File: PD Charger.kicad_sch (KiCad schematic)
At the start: 76 parts, among them J1 USB_C_Receptacle_USB2.0, J2 Conn_ARM_SWD_TagConnect_TC2030, J3 XT60_M, Q1 NMOS, Q2 NMOS, Q3 NMOS, Q4 NMOS, Q5 NTMFS002P03, Q6 NTMFS002P03, Q7 Q_Dual_NMOS_S1G1D2S2G2D1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

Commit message: values updated
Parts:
- C1: value Cin -> 82u
- C14, C15, C16, C17: value Cin -> 10u
- C18, C19, C20, C21, C27, C28: value Cout -> 10u
- C2: value Cout -> 82u
- C3, C4: value C -> 0.47u
- C34: value FF -> 20p
- J3: footprint Connector_AMASS:AMASS_XT60IPW-M_1x03_P7.20mm_Horizontal -> Connector_AMASS:AMASS_XT60PW-M_1x02_P7.20mm_Horizontal
- R1, R2, R3, R4: value R -> 1
- R10, R7: value Rup -> 100k
- R11: value Rdiv1 -> 36k
- R12: value Rdiv2 -> 9k
- R14, R17: value R -> 100k
- R15: value R -> 752
- R16, R18: value R -> 5820
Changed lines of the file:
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@@
       (effects (font (size 1.27 1.27)) (justify left))
     )
-    (property "Value" "Cout" (at 249.682 140.97 0)
+    (property "Value" "10u" (at 249.682 140.97 0)
       (effects (font (size 1.27 1.27)) (justify left))
     )
@@
       (effects (font (size 1.27 1.27)))
     )
-    (property "Value" "R" (at 81.28 59.69 90)
+    (property "Value" "1" (at 81.28 59.69 90)
       (effects (font (size 1.27 1.27)))
     )
@@
       (effects (font (size 1.27 1.27)))
     )
-    (property "Footprint" "Connector_AMASS:AMASS_XT60IPW-M_1x03_P7.20mm_Horizontal" (at 141.732 41.91 0)
+    (property "Footprint" "Connector_AMASS:AMASS_XT60PW-M_1x02_P7.20mm_Horizontal" (at 141.732 41.91 0)
       (effects (font (size 1.27 1.27)) hide)
     )
@@
       (effects (font (size 1.27 1.27)) (justify left))
     )
-    (property "Value" "Cin" (at 184.15 41.91 0)
+    (property "Value" "82u" (at 184.15 41.91 0)
       (effects (font (size 1.27 1.27)) (justify left))
     )
@@
       (effects (font (size 1.27 1.27)) (justify left))
     )
-    (property "Value" "Cout" (at 239.014 140.97 0)
+    (property "Value" "10u" (at 239.014 140.97 0)
       (effects (font (size 1.27 1.27)) (justify left))
     )
@@
       (effects (font (size 1.27 1.27)) (justify left))
     )
-    (property "Value" "R" (at 102.489 103.124 0)
+    (property "Value" "100k" (at 102.489 103.124 0)
       (effects (font (size 1.27 1.27)) (justify left))
     )
@@
       (effects (font (size 1.27 1.27)) (justify left))
     )
-    (property "Value" "Cout" (at 278.13 41.91 0)
+    (property "Value" "10u" (at 278.13 41.91 0)
       (effects (font (size 1.27 1.27)) (justify left))
     )
@@
       (effects (font (size 1.27 1.27)) (justify left))
     )
-    (property "Value" "R" (at 102.489 111.76 0)
+    (property "Value" "5820" (at 102.489 111.76 0)
       (effects (font (size 1.27 1.27)) (justify left))
     )
@@
       (effects (font (size 1.27 1.27)))
     )
-    (property "Value" "Rdiv1" (at 111.76 47.752 90)
+    (property "Value" "36k" (at 111.76 47.752 90)
       (effects (font (size 1.27 1.27)))
     )
@@
       (effects (font (size 1.27 1.27)) (justify left))
     )
-    (property "Value" "Cin" (at 176.53 41.91 0)
+    (property "Value" "10u" (at 176.53 41.91 0)
       (effects (font (size 1.27 1.27)) (justify left))
     )
@@
       (effects (font (size 1.27 1.27)) (justify left))
     )
-    (property "Value" "Cout" (at 255.27 41.91 0)
+    (property "Value" "10u" (at 255.27 41.91 0)
       (effects (font (size 1.27 1.27)) (justify left))
     )
@@
       (effects (font (size 1.27 1.27)) (justify left))
     )
-    (property "Value" "Cout" (at 247.65 41.91 0)
+    (property "Value" "82u" (at 247.65 41.91 0)
       (effects (font (size 1.27 1.27)) (justify left))
     )
@@
       (effects (font (size 1.27 1.27)))
     )
-    (property "Value" "R" (at 81.28 22.86 90)
+    (property "Value" "1" (at 81.28 22.86 90)
       (effects (font (size 1.27 1.27)))
     )
@@
       (effects (font (size 1.27 1.27)) (justify left))
     )
-    (property "Value" "Cin" (at 162.56 41.91 0)
+    (property "Value" "10u" (at 162.56 41.91 0)
       (effects (font (size 1.27 1.27)) (justify left))
     )
@@
       (effects (font (size 1.27 1.27)) (justify left))
     )
-    (property "Value" "C" (at 97.79 52.07 0)
+    (property "Value" "0.47u" (at 97.79 52.07 0)
       (effects (font (size 1.27 1.27)) (justify left))
     )
@@
       (effects (font (size 1.27 1.27)))
     )
-    (property "Value" "Rdiv2" (at 111.76 56.388 90)
+    (property "Value" "9k" (at 111.76 56.388 90)
       (effects (font (size 1.27 1.27)))
     )
@@
       (effects (font (size 1.27 1.27)) (justify left))
     )
-    (property "Value" "Rup" (at 49.53 25.4 0)
+    (property "Value" "100k" (at 49.53 25.4 0)
       (effects (font (size 1.27 1.27)) (justify left))
     )
@@
       (effects (font (size 1.27 1.27)) (justify left))
     )
-    (property "Value" "Cout" (at 270.51 41.91 0)
+    (property "Value" "10u" (at 270.51 41.91 0)
       (effects (font (size 1.27 1.27)) (justify left))
     )
@@
       (effects (font (size 1.27 1.27)) (justify left))
     )
-    (property "Value" "FF" (at 219.456 154.178 0)
+    (property "Value" "20p" (at 219.456 154.178 0)
       (effects (font (size 1.27 1.27)) (justify left))
     )
@@
       (effects (font (size 1.27 1.27)))
     )
-    (property "Value" "R" (at 81.28 40.64 90)
+    (property "Value" "1" (at 81.28 40.64 90)
       (effects (font (size 1.27 1.27)))
     )
@@
       (effects (font (size 1.27 1.27)) (justify left))
     )
-    (property "Value" "R" (at 115.697 103.124 0)
+    (property "Value" "100k" (at 115.697 103.124 0)
       (effects (font (size 1.27 1.27)) (justify left))
     )
@@
       (effects (font (size 1.27 1.27)) (justify left))
     )
-    (property "Value" "Cin" (at 156.21 41.91 0)
+    (property "Value" "10u" (at 156.21 41.91 0)
       (effects (font (size 1.27 1.27)) (justify left))
     )
@@
       (effects (font (size 1.27 1.27)) (justify left))
     )
-    (property "Value" "Cout" (at 262.89 41.91 0)
+    (property "Value" "10u" (at 262.89 41.91 0)
       (effects (font (size 1.27 1.27)) (justify left))
     )
@@
       (effects (font (size 1.27 1.27)))
     )
-    (property "Value" "R" (at 81.28 52.07 90)
+    (property "Value" "1" (at 81.28 52.07 90)
       (effects (font (size 1.27 1.27)))
     )
@@
       (effects (font (size 1.27 1.27)) (justify left))
     )
-    (property "Value" "Cin" (at 168.91 41.91 0)
+    (property "Value" "10u" (at 168.91 41.91 0)
       (effects (font (size 1.27 1.27)) (justify left))
     )
@@
       (effects (font (size 1.27 1.27)) (justify left))
     )
-    (property "Value" "R" (at 115.697 111.76 0)
+    (property "Value" "5820" (at 115.697 111.76 0)
       (effects (font (size 1.27 1.27)) (justify left))
     )
@@
       (effects (font (size 1.27 1.27)) (justify left))
     )
-    (property "Value" "C" (at 97.79 34.29 0)
+    (property "Value" "0.47u" (at 97.79 34.29 0)
       (effects (font (size 1.27 1.27)) (justify left))
     )
@@
       (effects (font (size 1.27 1.27)))
     )
-    (property "Value" "Rup" (at 33.02 33.02 90)
+    (property "Value" "100k" (at 33.02 33.02 90)
       (effects (font (size 1.27 1.27)))
     )
@@
       (effects (font (size 1.27 1.27)) (justify left))
     )
-    (property "Value" "R" (at 124.079 69.596 0)
-      (effects (font (size 1.27 1.27)) (justify left))
-    )
+    (property "Value" "752" (at 124.079 69.596 0)
+      (effects (font (size 1.27 1.27)) (justify left))
+    )

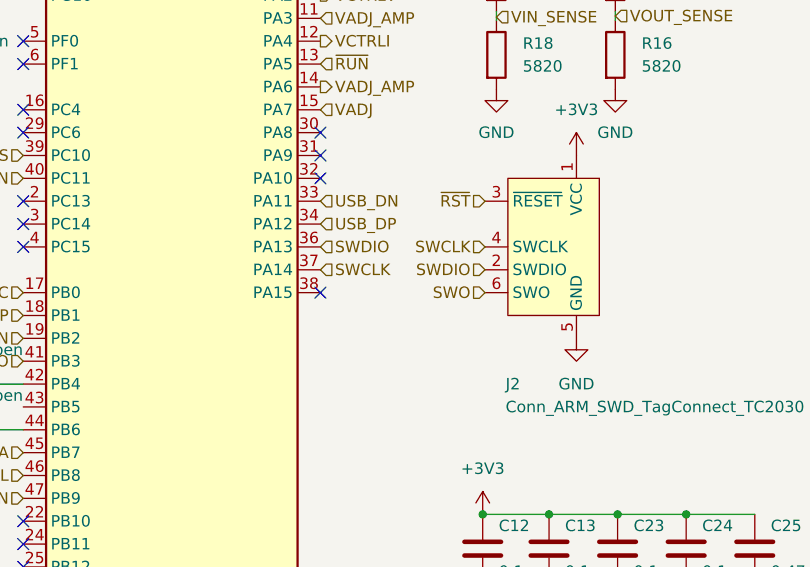
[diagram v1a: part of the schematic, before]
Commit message: DRC cleanup and added 3D models
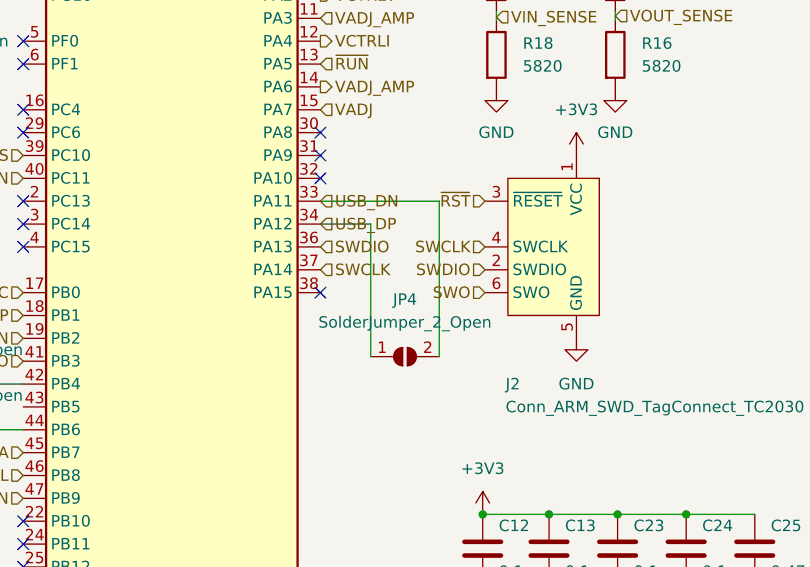
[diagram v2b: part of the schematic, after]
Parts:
- added JP4: SolderJumper_2_Open, Jumper:SolderJumper-2_P1.3mm_Open_RoundedPad1.0x1.5mm, symbol Jumper:SolderJumper_2_Open
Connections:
- net USB_DN: now also JP4.2 (B)
- net USB_DP: now also JP4.1 (A)
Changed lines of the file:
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@@
     (stroke (width 0) (type default))
   )
+  (wire (pts (xy 85.598 144.018) (xy 85.598 129.286))
+    (stroke (width 0) (type default))
+  )
   (wire (pts (xy 50.8 54.61) (xy 36.83 54.61))
     (stroke (width 0) (type default))
@@
     (stroke (width 0) (type default))
   )
+  (wire (pts (xy 93.218 144.018) (xy 93.218 126.746))
+    (stroke (width 0) (type default))
+  )
   (wire (pts (xy 153.416 135.89) (xy 164.084 135.89))
     (stroke (width 0) (type default))
@@
     (stroke (width 0) (type default))
   )
+  (wire (pts (xy 93.218 126.746) (xy 80.01 126.746))
+    (stroke (width 0) (type default))
+  )
   (wire (pts (xy 198.628 72.644) (xy 201.168 72.644))
     (stroke (width 0) (type default))
@@
     (stroke (width 0) (type default))
   )
+  (wire (pts (xy 85.598 129.286) (xy 80.01 129.286))
+    (stroke (width 0) (type default))
+  )
   (wire (pts (xy 180.34 53.34) (xy 199.39 53.34))
     (stroke (width 0) (type default))
@@
         )
       )
+    )
+  )
+  (symbol (lib_id "Jumper:SolderJumper_2_Open") (at 89.408 144.018 0) (unit 1)
+    (in_bom yes) (on_board yes) (dnp no) (fields_autoplaced)
+    (property "Reference" "JP4" (at 89.408 137.668 0)
+      (effects (font (size 1.27 1.27)))
+    )
+    (property "Value" "SolderJumper_2_Open" (at 89.408 140.208 0)
+      (effects (font (size 1.27 1.27)))
+    )
+    (property "Footprint" "Jumper:SolderJumper-2_P1.3mm_Open_RoundedPad1.0x1.5mm" (at 89.408 144.018 0)
+      (effects (font (size 1.27 1.27)) hide)
+    )
+    (property "Datasheet" "~" (at 89.408 144.018 0)
+      (effects (font (size 1.27 1.27)) hide)
+    )
+    (pin "1")
+    (pin "2")
+    (instances
+      (project "PD Charger"
+        (path "/2223e2d2-71c8-4f08-b970-c0182a3b98e5"
+          (reference "JP4") (unit 1)
+        )
+      )

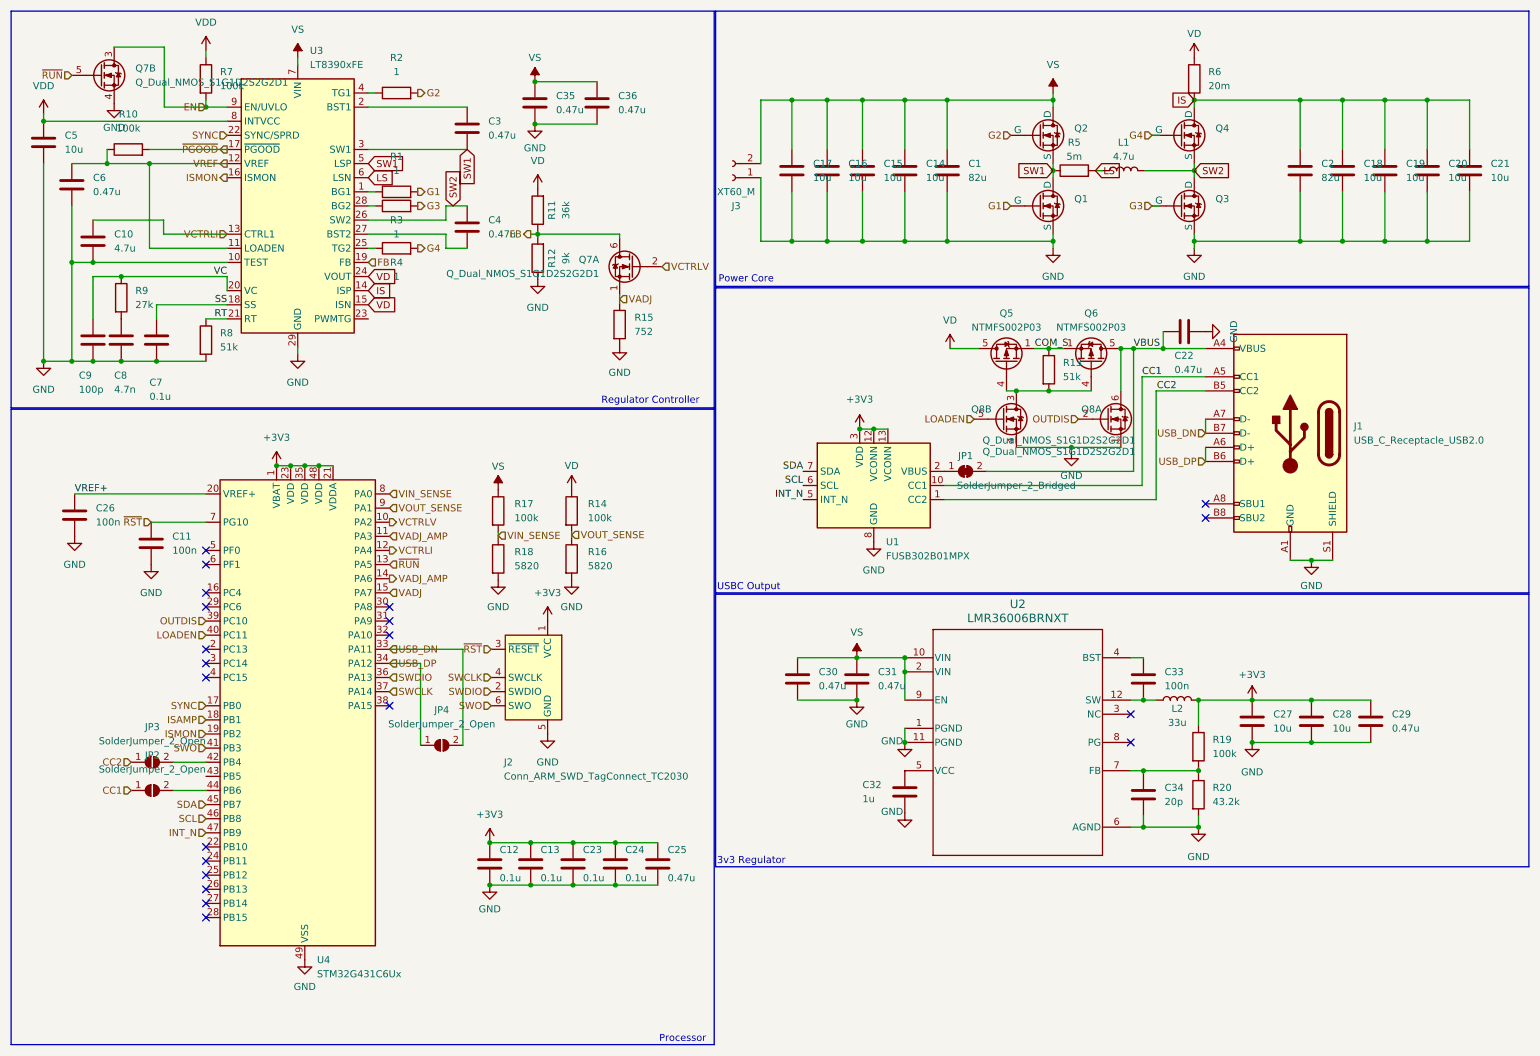
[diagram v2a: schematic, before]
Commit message: silkscreen and testpoints
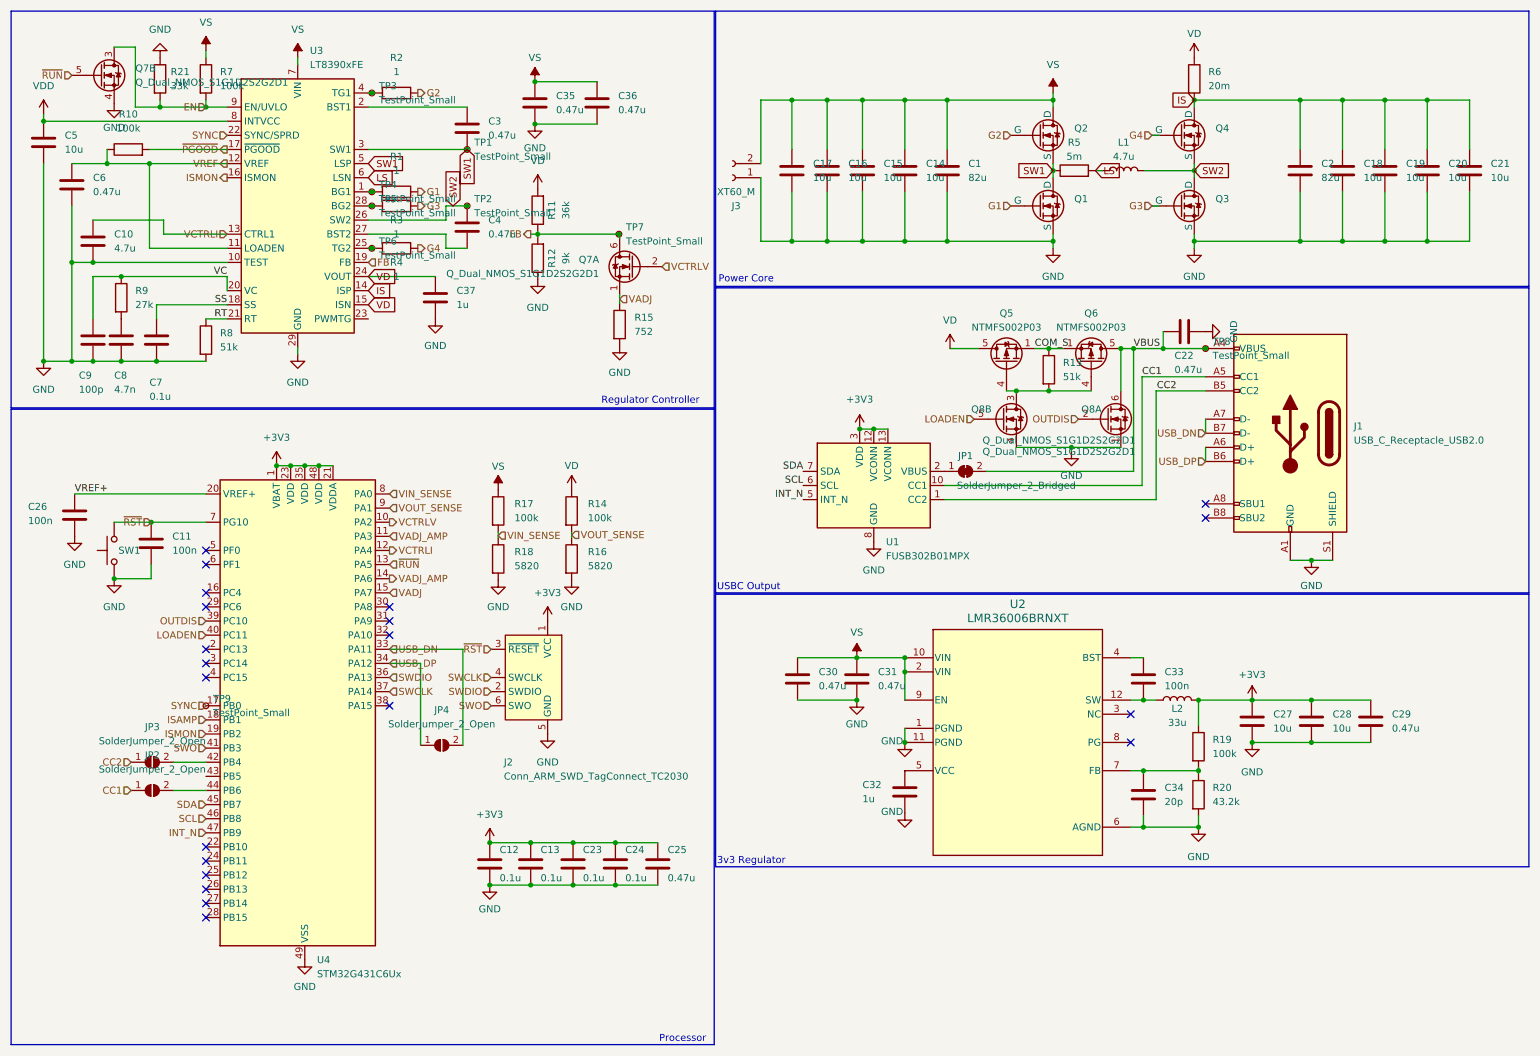
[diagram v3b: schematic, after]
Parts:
- added C37: 1u, Capacitor_SMD:C_0603_1608Metric, symbol Device:C
- added R21: 33k, Resistor_SMD:R_0603_1608Metric, symbol Device:R
- added SW1: SW_MEC_5G, Button_Switch_SMD:SW_SPST_B3U-1000P-B, symbol Switch:SW_Push
- added TP1, TP2, TP3, TP4, TP5, TP6, TP7, TP8, TP9: TestPoint_Small, TestPoint:TestPoint_Pad_D1.0mm, symbol Connector:TestPoint_Small
- J2: footprint Connector:Tag-Connect_TC2030-IDC-FP_2x03_P1.27mm_Vertical -> Connector:Tag-Connect_TC2030-IDC-NL_2x03_P1.27mm_Vertical
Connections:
- net EN: now also R21.2
- net FB: now also TP7.1
- net GND: now also C37.2, R21.1, SW1.1
- net SW1: now also TP1.1
- net SW2: now also TP2.1
- net SYNC: now also TP9.1
- net VBUS: now also TP8.1
- net VD: now also C37.1
- net VDD: no longer R7.1
- net VS: now also R7.1
- net ~{RST}: now also SW1.2
- net at R4.1, U3.25 (TG2): now also TP6.1
- net at R1.1, U3.1 (BG1): now also TP4.1
- net at R3.1, U3.28 (BG2): now also TP5.1
- net at R2.1, U3.4 (TG1): now also TP3.1
